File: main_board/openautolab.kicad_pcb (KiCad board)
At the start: 2 copper layers, 144.8 x 88.9 mm, 35 parts, among them J1 PIN11, J10 HX711, J11 LCD, J16 PWR_IN, J17 FILTER_PUMP, J18 FILTER_SENSOR, J2 PIN9, J3 PIN10, J4 PIN12, J6 PIN7, J7 PIN8, J8 PUMP, J9 SERVO, K1 FINDER-36.11, K2 FINDER-36.11, SW0 PIN_A0, SW1 PIN_A1, SW2 PIN_A2, SW3 SW_DPST_x2, SW4 SW_DPST_x2, U1 TD62064APG, U2 TD62064APG, U3 LM2576T-5

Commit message: update board
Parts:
- removed BZ0: Buzzer, Buzzer_Beeper:Buzzer_12x9.5RM7.6
- removed J16: PWR_IN, TerminalBlock_Phoenix:TerminalBlock_Phoenix_MKDS-3-2-5.08_1x02_P5.08mm_Horizontal
- removed J17: FILTER_PUMP, TerminalBlock_Phoenix:TerminalBlock_Phoenix_MKDS-3-2-5.08_1x02_P5.08mm_Horizontal
- removed J18: FILTER_SENSOR, TerminalBlock_Phoenix:TerminalBlock_Phoenix_MKDS-3-2-5.08_1x02_P5.08mm_Horizontal
- removed K1, K2: FINDER-36.11, Relay_THT:Relay_SPDT_Finder_36.11
- removed NT1: NetTie_2, NetTie:NetTie-2_SMD_Pad2.0mm
- removed U3: LM2576T-5, Package_TO_SOT_THT:TO-220-5_Vertical
- added D10: 1N5819WS, Diode_SMD:D_SOD-323, F.Cu at (138.7, 49.5)
- added D7: 1N5819WS, Diode_SMD:D_SOD-323, F.Cu at (99.1, 49.5)
- added D8: 1N5819WS, Diode_SMD:D_SOD-323, F.Cu at (91.4, 81.5)
- added D9: 1N5819, Diode_SMD:D_SOD-323, F.Cu at (90.2, 49.5)
- added J12: PWR_IN, TerminalBlock_Phoenix:TerminalBlock_Phoenix_MKDS-3-2-5.08_1x02_P5.08mm_Horizontal, F.Cu at (134.6, 90.2)
- added J13: HX711, Connector_PinSocket_2.54mm:PinSocket_1x04_P2.54mm_Vertical, F.Cu at (54.6, 90.2)
- added J14: SERVO, Connector_PinSocket_2.54mm:PinSocket_1x03_P2.54mm_Vertical, F.Cu at (38.1, 69.8)
- added J15: LCD, Connector_PinSocket_2.54mm:PinSocket_1x04_P2.54mm_Vertical, F.Cu at (48.3, 71.1)
- added J5: PIN9, TerminalBlock_Phoenix:TerminalBlock_Phoenix_PT-1,5-2-3.5-H_1x02_P3.50mm_Horizontal, F.Cu at (78.7, 43.2)
- added Q1: TSM2302CX, Package_TO_SOT_SMD:SOT-23, F.Cu at (44.5, 53.0)
- added Q2: TSM2302CX, Package_TO_SOT_SMD:SOT-23, F.Cu at (52.1, 53.0)
- added Q3: TSM2302CX, Package_TO_SOT_SMD:SOT-23, F.Cu at (61.2, 53.0)
- added Q4: TSM2302CX, Package_TO_SOT_SMD:SOT-23, F.Cu at (70.1, 53.0)
- added Q5: TSM2302CX, Package_TO_SOT_SMD:SOT-23, F.Cu at (79.0, 53.0)
- added Q6: TSM2302CX, Package_TO_SOT_SMD:SOT-23, F.Cu at (87.9, 53.0)
- added Q7: TSM2302CX, Package_TO_SOT_SMD:SOT-23, F.Cu at (96.8, 53.0)
- added Q8: TSM2302CX, Package_TO_SOT_SMD:SOT-23, F.Cu at (105.7, 53.0)
- added R1: 10k, Resistor_SMD:R_0603_1608Metric, F.Cu at (44.3, 56.5)
- added R10: 10k, Resistor_SMD:R_0603_1608Metric, F.Cu at (78.9, 56.5)
- added R11: 100, Resistor_SMD:R_0603_1608Metric, F.Cu at (87.8, 58.6)
- added R12: 10k, Resistor_SMD:R_0603_1608Metric, F.Cu at (87.8, 56.5)
- added R13: 100, Resistor_SMD:R_0603_1608Metric, F.Cu at (96.7, 59.0)
- added R14: 10k, Resistor_SMD:R_0603_1608Metric, F.Cu at (96.7, 56.5)
- added R15: 100, Resistor_SMD:R_0603_1608Metric, F.Cu at (105.6, 59.0)
- added R16: 10k, Resistor_SMD:R_0603_1608Metric, F.Cu at (105.6, 56.5)
- added R2: 100, Resistor_SMD:R_0603_1608Metric, F.Cu at (44.3, 59.0)
- added R3: 100, Resistor_SMD:R_0603_1608Metric, F.Cu at (51.9, 59.0)
- added R4: 10k, Resistor_SMD:R_0603_1608Metric, F.Cu at (51.9, 56.5)
- added R5: 100, Resistor_SMD:R_0603_1608Metric, F.Cu at (61.1, 59.0)
- added R6: 10k, Resistor_SMD:R_0603_1608Metric, F.Cu at (61.1, 56.5)
- added R7: 100, Resistor_SMD:R_0603_1608Metric, F.Cu at (70.0, 59.0)
- added R8: 10k, Resistor_SMD:R_0603_1608Metric, F.Cu at (70.0, 56.5)
- added R9: 100, Resistor_SMD:R_0603_1608Metric, F.Cu at (78.9, 59.0)
- C1: value C_Polarized -> 100; footprint Capacitor_THT:CP_Radial_D10.0mm_P5.00mm -> Capacitor_SMD:CP_Elec_6.3x5.4
- C2: value C_Polarized -> 330; footprint Capacitor_THT:CP_Radial_D8.0mm_P5.00mm -> Capacitor_SMD:CP_Elec_8x10
- D1, D2, D3, D4, D5: value 1N4004 -> 1N5819WS; footprint Diode_THT:D_DO-41_SOD81_P10.16mm_Horizontal -> Diode_SMD:D_SOD-323
- D6: value 1N5822 -> 1N5819WS; footprint Diode_THT:D_DO-201AD_P15.24mm_Horizontal -> Diode_SMD:D_SOD-323
- J1: value PIN11 -> PIN13; footprint TerminalBlock_Phoenix:TerminalBlock_Phoenix_MKDS-3-2-5.08_1x02_P5.08mm_Horizontal -> TerminalBlock_Phoenix:TerminalBlock_Phoenix_PT-1,5-2-3.5-H_1x02_P3.50mm_Horizontal
- J10: value HX711 -> FILTER_PUMP; footprint Connector_PinSocket_2.54mm:PinSocket_1x04_P2.54mm_Vertical -> TerminalBlock_Phoenix:TerminalBlock_Phoenix_MKDS-3-2-5.08_1x02_P5.08mm_Horizontal
- J11: value LCD -> FILTER_SENSOR; footprint Connector_PinSocket_2.54mm:PinSocket_1x04_P2.54mm_Vertical -> TerminalBlock_Phoenix:TerminalBlock_Phoenix_MKDS-3-2-5.08_1x02_P5.08mm_Horizontal
- J2: value PIN9 -> PIN12; footprint TerminalBlock_Phoenix:TerminalBlock_Phoenix_MKDS-3-2-5.08_1x02_P5.08mm_Horizontal -> TerminalBlock_Phoenix:TerminalBlock_Phoenix_PT-1,5-2-3.5-H_1x02_P3.50mm_Horizontal
- J3: value PIN10 -> PIN11; footprint TerminalBlock_Phoenix:TerminalBlock_Phoenix_MKDS-3-2-5.08_1x02_P5.08mm_Horizontal -> TerminalBlock_Phoenix:TerminalBlock_Phoenix_PT-1,5-2-3.5-H_1x02_P3.50mm_Horizontal
- J4: value PIN12 -> PIN10; footprint TerminalBlock_Phoenix:TerminalBlock_Phoenix_MKDS-3-2-5.08_1x02_P5.08mm_Horizontal -> TerminalBlock_Phoenix:TerminalBlock_Phoenix_PT-1,5-2-3.5-H_1x02_P3.50mm_Horizontal
- J6: value PIN7 -> PIN8; footprint TerminalBlock_Phoenix:TerminalBlock_Phoenix_MKDS-3-2-5.08_1x02_P5.08mm_Horizontal -> TerminalBlock_Phoenix:TerminalBlock_Phoenix_PT-1,5-2-3.5-H_1x02_P3.50mm_Horizontal
- J7: value PIN8 -> PIN7; footprint TerminalBlock_Phoenix:TerminalBlock_Phoenix_MKDS-3-2-5.08_1x02_P5.08mm_Horizontal -> TerminalBlock_Phoenix:TerminalBlock_Phoenix_PT-1,5-2-3.5-H_1x02_P3.50mm_Horizontal
- J8: value PUMP -> PINA0; footprint TerminalBlock_Phoenix:TerminalBlock_Phoenix_MKDS-3-2-5.08_1x02_P5.08mm_Horizontal -> TerminalBlock_Phoenix:TerminalBlock_Phoenix_PT-1,5-2-3.5-H_1x02_P3.50mm_Horizontal
- J9: value SERVO -> PUMP; footprint Connector_PinSocket_2.54mm:PinSocket_1x03_P2.54mm_Vertical -> TerminalBlock_Phoenix:TerminalBlock_Phoenix_MKDS-3-2-5.08_1x02_P5.08mm_Horizontal
- L1: value L -> 330; footprint Inductor_THT:L_Toroid_Vertical_L26.7mm_W14.0mm_P10.16mm_Pulse_D -> Inductor_SMD:L_12x12mm_H8mm
- SW0, SW1, SW2: footprint Button_Switch_THT:SW_PUSH_6mm -> Button_Switch_SMD:SW_Push_1P1T_NO_6x6mm_H9.5mm
- U1: value TD62064APG -> DRV8870DDA; footprint Package_DIP:DIP-16_W7.62mm -> Package_SO:Texas_HTSOP-8-1EP_3.9x4.9mm_P1.27mm_EP2.95x4.9mm_Mask2.4x3.1mm_ThermalVias
- U2: value TD62064APG -> LM2575-5.0BU; footprint Package_DIP:DIP-16_W7.62mm -> Package_TO_SOT_SMD:TO-263-5_TabPin3
- moved L1 91.4 mm to (85.1, 92.7), turned to 0 degrees
- moved D1 85.3 mm to (44.7, 49.5), turned to 180 degrees
- moved D2 83.0 mm to (53.3, 49.5), turned to 180 degrees
- moved J9 79.0 mm to (115.6, 46.0), turned to 0 degrees
- moved J10 72.9 mm to (128.3, 46.0), turned to 0 degrees
- moved C1 65.1 mm to (82.5, 80.0)
- moved SW4 62.0 mm to (137.2, 101.6), turned to 90 degrees
- moved D5 61.7 mm to (81.1, 49.5), turned to 180 degrees
- moved J11 56.0 mm to (134.6, 57.1), turned to -90 degrees
- moved U2 55.2 mm to (105.1, 94.2)
- moved D3 55.1 mm to (62.2, 49.5), turned to 180 degrees
- moved D4 51.5 mm to (72.2, 49.5), turned to 180 degrees
- moved U1 48.6 mm to (116.8, 60.3), turned to 90 degrees
- moved C2 48.0 mm to (120.7, 94.7), turned to -90 degrees
- moved A1 45.2 mm to (100.3, 83.8)
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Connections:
- A1 pad 22: unconnected-(A1-A3-Pad22) -> Net-(A1-A3)
- D2 pad 1: Net-(D1-A) -> +12V
- D2 pad 2: GNDPWR -> Net-(D2-A)
- D4 pad 1: Net-(D3-A) -> +12V
- D4 pad 2: GNDPWR -> Net-(D4-A)
- D6 pad 1: Net-(D6-K) -> +12V
- D6 pad 2: GND -> Net-(D6-A)
- J1 pad 1: Net-(J1-Pin_1) -> Net-(D1-A)
- J10 pad 1: GND -> Net-(D10-A)
- J10 pad 2: Net-(A1-D3) -> +12V
- J11 pad 2: +5V -> Net-(J11-Pin_2)
- J2 pad 1: Net-(J2-Pin_1) -> Net-(D2-A)
- J3 pad 1: Net-(J3-Pin_1) -> Net-(D3-A)
- J4 pad 1: Net-(J4-Pin_1) -> Net-(D4-A)
- J6 pad 1: Net-(J6-Pin_1) -> Net-(D6-A)
- J7 pad 1: Net-(J7-Pin_1) -> Net-(D7-A)
- J8 pad 1: Net-(D3-A) -> Net-(D8-A)
- J8 pad 2: Net-(D1-A) -> +12V
- J9 pad 1: GND -> Net-(J9-Pin_1)
- J9 pad 2: +5V -> Net-(J9-Pin_2)
- L1 pad 1: Net-(D6-K) -> Net-(D9-K)
- SW0 pad 1: Net-(A1-A0) -> Net-(A1-A3)
- SW1 pad 1: Net-(A1-A1) -> Net-(A1-A2)
- SW2 pad 1: Net-(A1-A2) -> Net-(A1-A1)
- SW3 pad 1: Net-(D5-A) -> Net-(D10-A)
- SW3 pad 2: Net-(J18-Pin_2) -> Net-(J11-Pin_2)
- U1 pad 1: +12V -> GND
- U1 pad 2: Net-(J6-Pin_1) -> Net-(A1-D12)
- U1 pad 3: Net-(A1-D7) -> Net-(A1-D13)
- U1 pad 4: GNDPWR -> +5V
- U1 pad 5: GNDPWR -> +12V
- U1 pad 6: Net-(A1-D5) -> Net-(J9-Pin_2)
- U1 pad 7: Net-(U1-O2) -> GND
- U1 pad 8: (no net) -> Net-(J9-Pin_1)
- U1 pad 9: Net-(U1-O3) -> GND
- U2 pad 1: +12V -> +5V
- U2 pad 2: Net-(J1-Pin_1) -> GND
- U2 pad 3: Net-(A1-D11) -> GND
- U2 pad 4: GNDPWR -> +12V
- U2 pad 5: GNDPWR -> Net-(D9-K)
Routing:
- net GNDPWR: track 185.2 -> 0.00 mm, vias 1 -> 0
- net GND: track 306.1 -> 466.2 mm
- net Net-(A1-D12): track 145.2 -> 29.7 mm, vias 1 -> 0
- net Net-(A1-D10): track 150.9 -> 52.3 mm, vias 0 -> 1
- net Net-(A1-D11): track 133.4 -> 37.6 mm, vias 2 -> 0
- net Net-(A1-A3): track 0.00 -> 90.3 mm, vias 0 -> 1
- net Net-(A1-D9): track 133.7 -> 50.6 mm, vias 1 -> 0
- net Net-(D9-K): track 0.00 -> 74.4 mm, vias 0 -> 2
- net Net-(J7-Pin_1): track 73.5 -> 0.00 mm
- net Net-(D1-A): track 76.3 -> 9.42 mm
- net Net-(A1-D8): track 119.8 -> 57.2 mm, vias 1 -> 0
- net Net-(J4-Pin_1): track 61.9 -> 0.00 mm
- net Net-(D8-A): track 0.00 -> 52.1 mm, vias 0 -> 1
- net Net-(A1-D4): track 135.7 -> 85.8 mm
- net Net-(U1-O2): track 45.4 -> 0.00 mm
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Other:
- board size 144.8 x 88.9 mm -> 109.2 x 74.9 mm

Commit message: update schematic, complete parts description
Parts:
- removed D2, D3, D4, D5, D6, D7, D8: 1N5819WS, Diode_SMD:D_SOD-323
- removed D9: 1N5819, Diode_SMD:D_SOD-323
- removed Q1, Q2, Q3, Q4, Q5, Q6, Q7, Q8: TSM2302CX, Package_TO_SOT_SMD:SOT-23
- removed R1, R10, R12, R14, R16, R4, R6, R8: 10k, Resistor_SMD:R_0603_1608Metric
- removed R11, R13, R15, R2, R3, R5, R7, R9: 100, Resistor_SMD:R_0603_1608Metric
- added IC1: ULN2065B, Package_DIP:DIP-16_W7.62mm, F.Cu at (52.1, 54.6)
- added IC3: ULN2065B, Package_DIP:DIP-16_W7.62mm, F.Cu at (71.1, 54.6)
- C1: footprint Capacitor_SMD:CP_Elec_6.3x5.4 -> Capacitor_THT:CP_Radial_D8.0mm_P5.00mm
- C2: footprint Capacitor_SMD:CP_Elec_8x10 -> Capacitor_THT:CP_Radial_D8.0mm_P5.00mm
- D1, D10: footprint Diode_SMD:D_SOD-323 -> Diode_THT:D_A-405_P7.62mm_Horizontal
- J1: value PIN13 -> PIN11
- J2: value PIN12 -> PIN10
- J3: value PIN11 -> PIN9
- J4: value PIN10 -> PIN8
- J5: value PIN9 -> PIN7
- J6: value PIN8 -> PIN6
- J7: value PIN7 -> PIN5
- L1: footprint Inductor_SMD:L_12x12mm_H8mm -> Inductor_THT:L_Radial_D12.0mm_P5.00mm_Fastron_11P
- SW0, SW1, SW2: footprint Button_Switch_SMD:SW_Push_1P1T_NO_6x6mm_H9.5mm -> Button_Switch_THT:SW_PUSH_6mm
- U1: value DRV8870DDA -> ~; footprint Package_SO:Texas_HTSOP-8-1EP_3.9x4.9mm_P1.27mm_EP2.95x4.9mm_Mask2.4x3.1mm_ThermalVias -> Pololu_breakout_DRV8874:Pololu_breakout_DRV8874
- U2: value LM2575-5.0BU -> LM2575-5.0BT; footprint Package_TO_SOT_SMD:TO-263-5_TabPin3 -> Package_TO_SOT_THT:TO-220-5_P3.4x3.7mm_StaggerOdd_Lead3.8mm_Vertical
- moved D1 87.5 mm to (116.8, 99.1), turned to 90 degrees
- moved J15 40.8 mm to (88.9, 74.9)
- moved J4 35.6 mm to (105.4, 43.2)
- moved J8 35.6 mm to (69.8, 43.2)
- moved J1 35.6 mm to (78.7, 43.2)
- moved J2 35.6 mm to (87.6, 43.2)
- moved J3 35.6 mm to (96.5, 43.2)
- moved J5 35.6 mm to (43.2, 43.2)
- moved J6 35.6 mm to (52.1, 43.2)
- moved J7 35.6 mm to (61.0, 43.2)
- moved L1 23.2 mm to (108.0, 96.6), turned to -90 degrees
- moved D10 22.4 mm to (116.8, 54.6), turned to 0 degrees
- moved U1 14.1 mm to (102.9, 58.4)
- moved C1 14.0 mm to (84.0, 94.0)
- moved U2 13.1 mm to (92.7, 98.3), turned to 0 degrees
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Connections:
- A1 pad 4: GND -> unconnected-(A1-GND-Pad4)
- D1 pad 1: +12V -> Net-(D1-K)
- D1 pad 2: Net-(D1-A) -> GND
- J1 pad 1: Net-(D1-A) -> Net-(IC3-O1)
- J11 pad 1: GND -> Net-(J11-Pin_1)
- J11 pad 2: Net-(J11-Pin_2) -> GND
- L1 pad 1: Net-(D9-K) -> Net-(D1-K)
- SW3 pad 2: Net-(J11-Pin_2) -> Net-(J11-Pin_1)
- U1 pad 1: GND -> unconnected-(U1-VM-Pad1)
- U1 pad 2: Net-(A1-D12) -> GND
- U1 pad 3: Net-(A1-D13) -> Net-(A1-D12)
- U1 pad 4: +5V -> Net-(A1-D13)
- U1 pad 5: +12V -> +5V
- U1 pad 6: Net-(J9-Pin_2) -> +5V
- U1 pad 7: GND -> unconnected-(U1-VREF-Pad7)
- U1 pad 8: Net-(J9-Pin_1) -> unconnected-(U1-CS-Pad8)
- U1 pad 9: GND -> unconnected-(U1-FAULT-Pad9)
- U2 pad 5: Net-(D9-K) -> Net-(D1-K)
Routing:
- net +12V: track 289.3 -> 400.1 mm
- net Net-(A1-D7): track 63.9 -> 154.2 mm, vias 2 -> 0
- net Net-(A1-A1): track 43.7 -> 129.2 mm, vias 1 -> 2
- net Net-(A1-D6): track 71.2 -> 146.9 mm, vias 2 -> 0
- net Net-(D9-K): track 74.4 -> 0.00 mm, vias 2 -> 0
- net Net-(A1-A2): track 57.2 -> 101.3 mm, vias 1 -> 2
- net Net-(A1-A5): track 71.5 -> 29.8 mm, vias 1 -> 0
- net Net-(A1-A4): track 73.6 -> 32.4 mm, vias 1 -> 0
- net Net-(A1-D11): track 37.6 -> 75.9 mm
- net Net-(IC1-O4): track 52.1 -> 15.6 mm, vias 1 -> 0
- net Net-(A1-D12): track 29.7 -> 62.4 mm
- net GND: track 466.2 -> 436.7 mm, vias 1 -> 10
- net Net-(IC3-O2): track 9.07 -> 38.0 mm
- net +5V: track 163.8 -> 192.5 mm, vias 2 -> 4
- net Net-(A1-D8): track 57.2 -> 83.6 mm
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
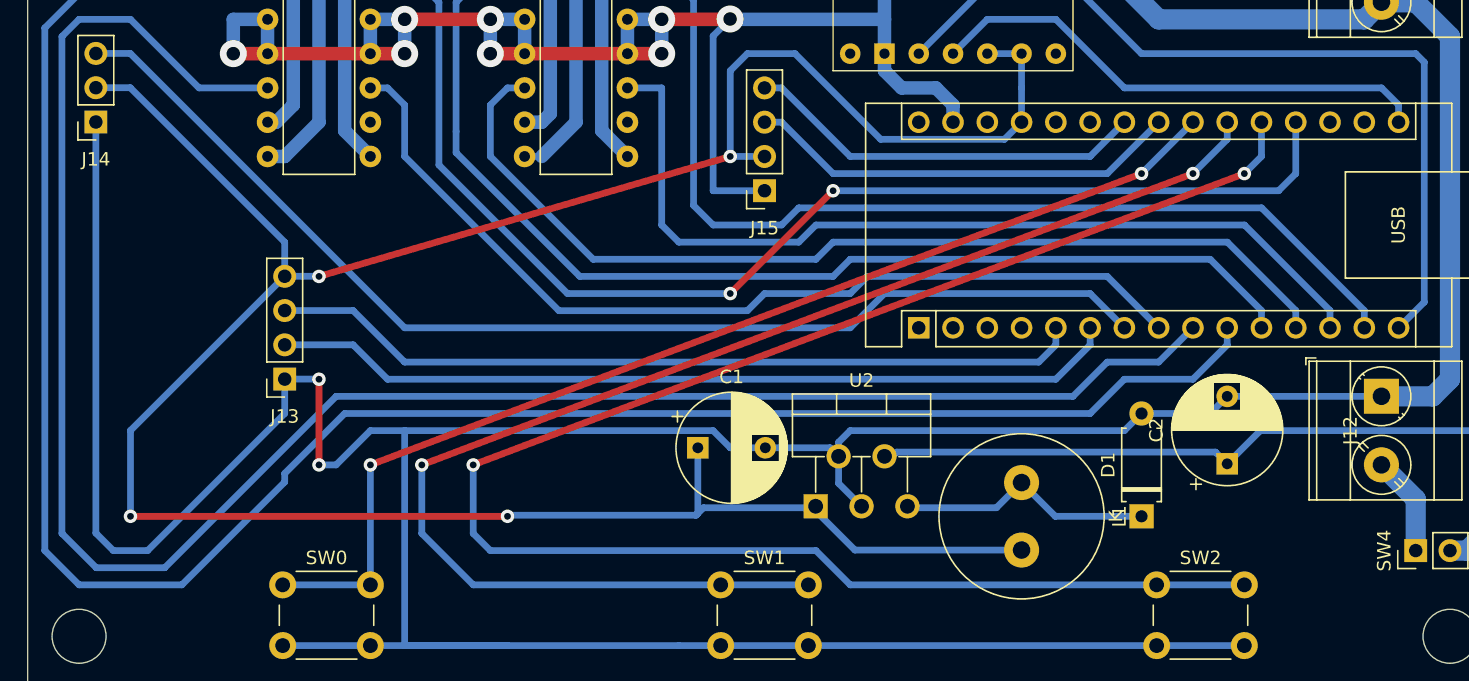
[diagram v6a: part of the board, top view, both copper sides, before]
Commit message: fixed error in board
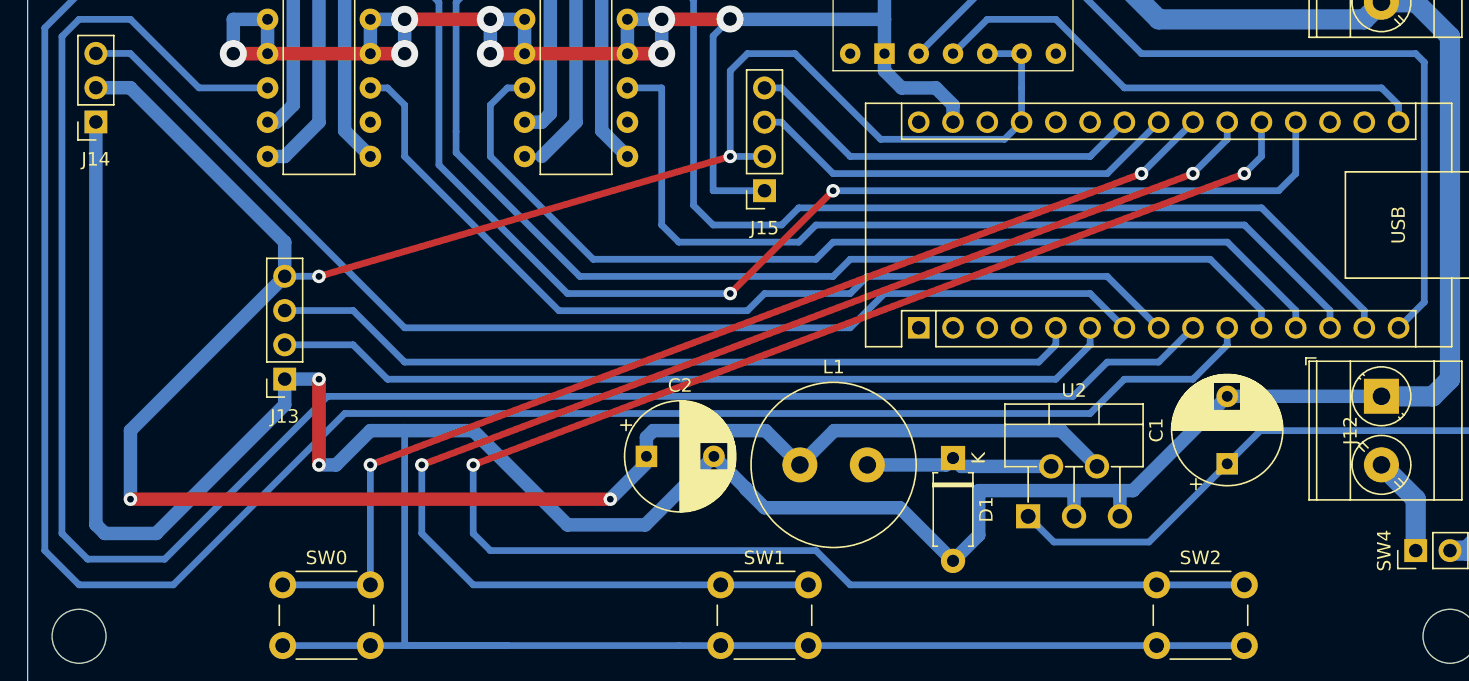
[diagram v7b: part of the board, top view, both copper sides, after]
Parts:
- moved C2 43.0 mm to (80.1, 94.6), turned to 0 degrees
- moved C1 39.3 mm to (123.2, 95.2), turned to 90 degrees
- moved L1 16.5 mm to (91.5, 95.2), turned to 0 degrees
- moved U2 15.8 mm to (108.4, 99.1)
- moved D1 14.6 mm to (102.9, 94.7), turned to -90 degrees
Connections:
- C1 pad 1: +5V -> +12V
- C2 pad 1: +12V -> +5V
- L1 pad 1: Net-(D1-K) -> +5V
- L1 pad 2: +5V -> Net-(D1-K)
- U2 pad 1: +5V -> +12V
- U2 pad 2: GND -> Net-(D1-K)
- U2 pad 4: +12V -> +5V
- U2 pad 5: Net-(D1-K) -> GND
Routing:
- net GND: track 436.7 -> 446.5 mm
- net +12V: track 400.1 -> 391.9 mm
- net Net-(D1-K): track 19.2 -> 14.1 mm
- net +5V: track 192.5 -> 196.6 mm
- net Net-(A1-D6): track 146.9 -> 146.4 mm

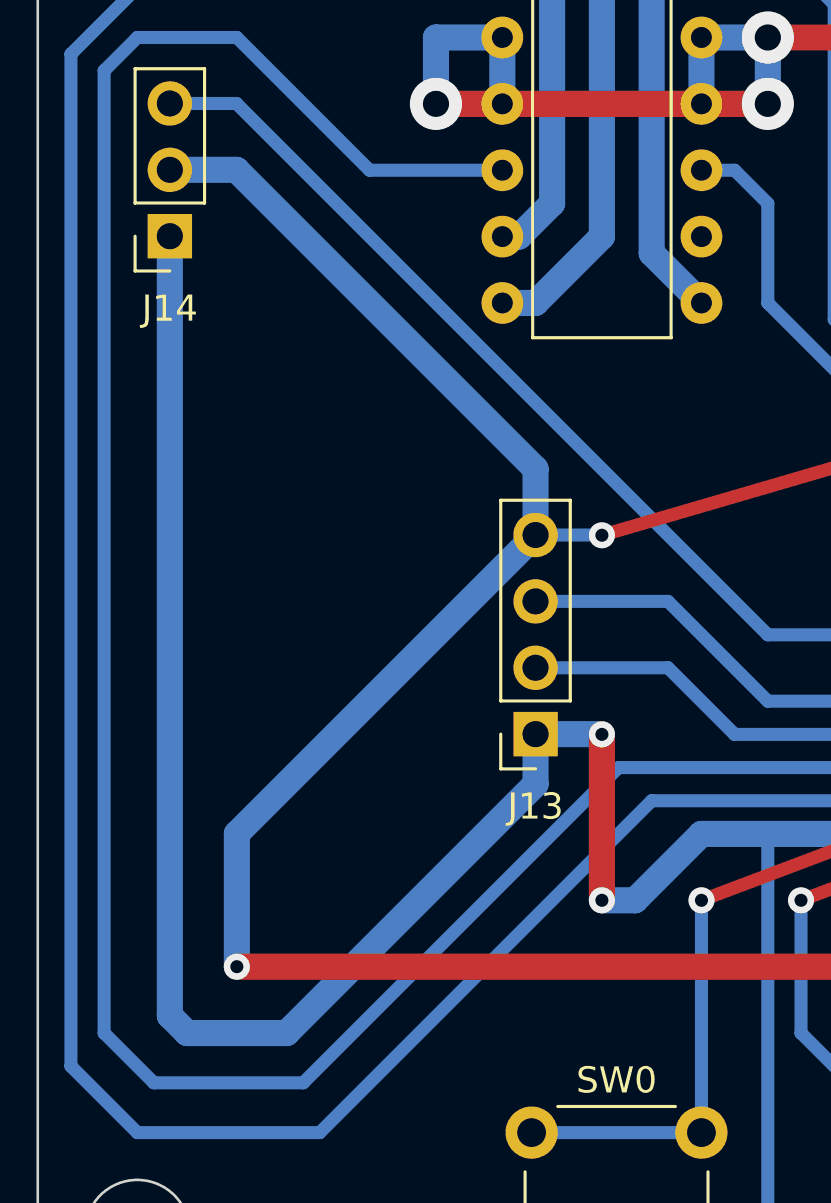
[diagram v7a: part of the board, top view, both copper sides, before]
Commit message: more accessible valves, small changes in enclosure
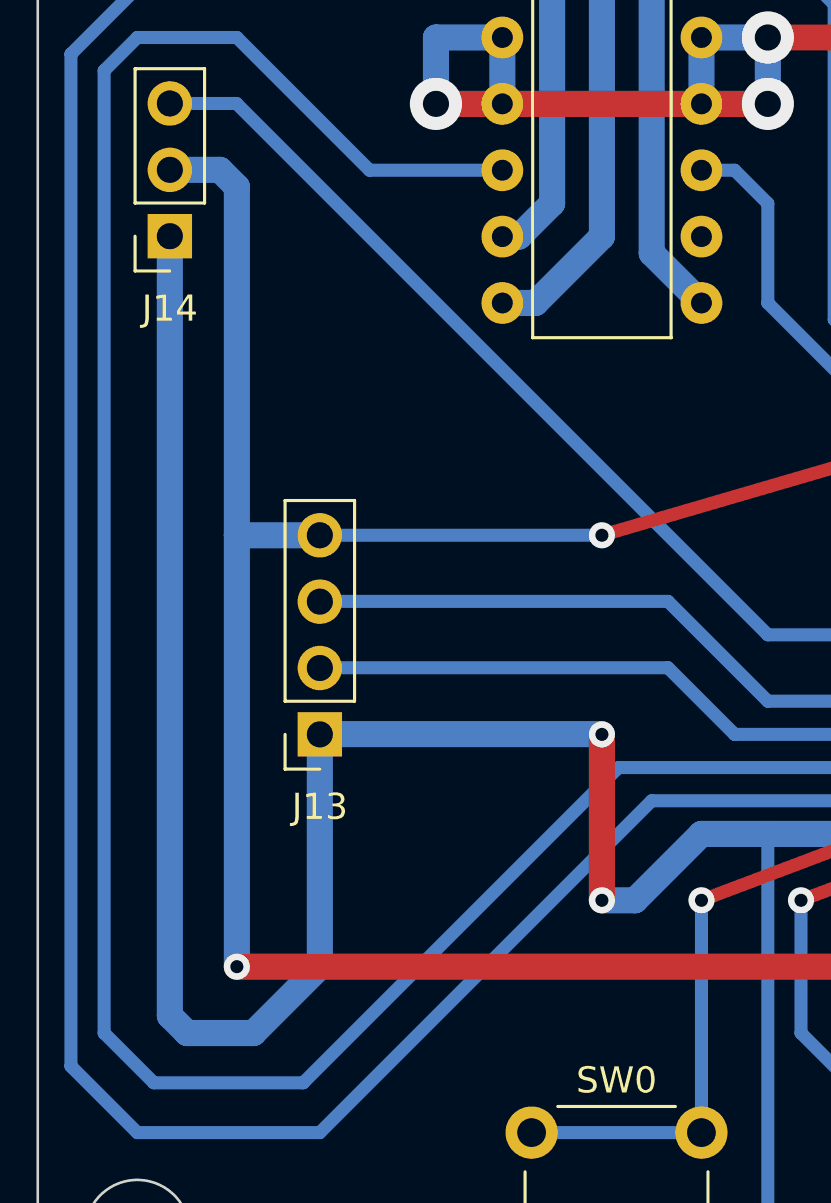
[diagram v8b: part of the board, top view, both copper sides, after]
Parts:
- J1: value PIN11 -> PIN8
- J2: value PIN10 -> PIN9
- J3: value PIN9 -> PIN10
- J4: value PIN8 -> PIN11
- SW0: value PIN_A0 -> PIN_A3
- SW1: value PIN_A1 -> PIN_A2
- SW2: value PIN_A2 -> PIN_A1
- moved J13 8.26 mm to (45.1, 88.9)
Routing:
- net Net-(A1-D3): track 63.1 -> 71.3 mm
- net Net-(A1-D2): track 60.5 -> 68.8 mm
- net GND: track 446.5 -> 450.5 mm
- net +5V: track 196.6 -> 198.2 mm
